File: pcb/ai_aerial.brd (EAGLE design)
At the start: 73 x 73 mm, 34 parts

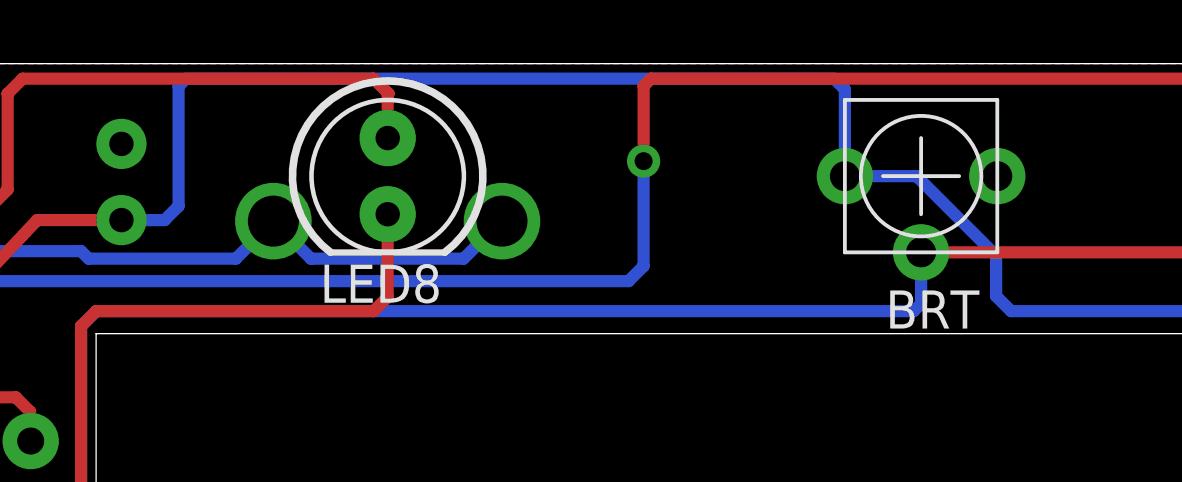
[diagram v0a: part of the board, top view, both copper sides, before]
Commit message: fixing trace error
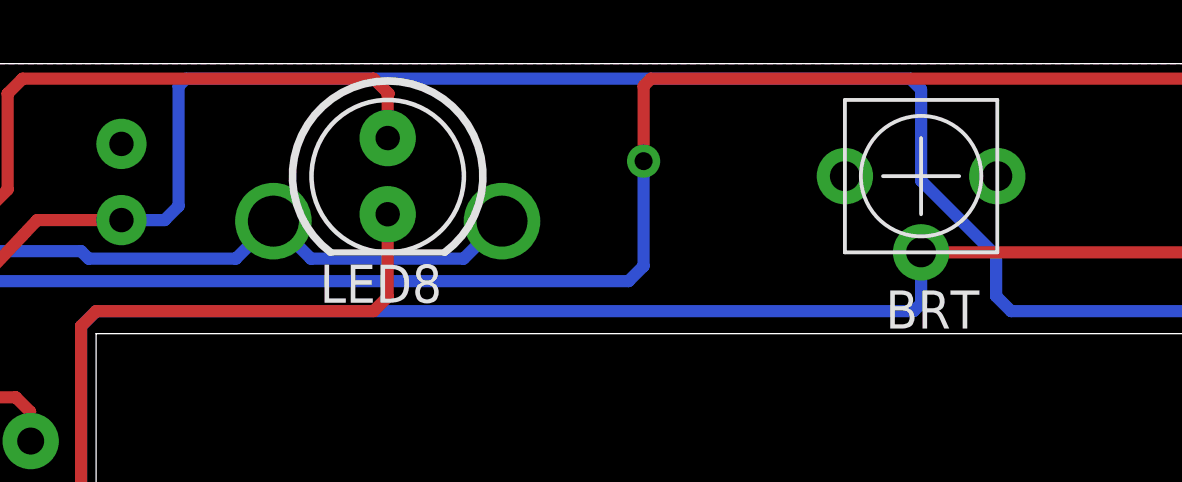
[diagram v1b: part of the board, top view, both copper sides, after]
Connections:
- net VBAT: no longer BRT.3
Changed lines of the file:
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@@
 <?xml version="1.0" encoding="utf-8"?>
 <!DOCTYPE eagle SYSTEM "eagle.dtd">
-<eagle version="7.1.0">
+<eagle version="6.5.0">
 <drawing>
 <settings>
@@
 <pass name="Default">
 <param name="RoutingGrid" value="50mil"/>
-<param name="AutoGrid" value="1"/>
-<param name="Efforts" value="0"/>
-<param name="TopRouterVariant" value="1"/>
 <param name="tpViaShape" value="round"/>
 <param name="PrefDir.1" value="|"/>
@@
 <contactref element="R5" pad="P$2"/>
 <contactref element="Q4" pad="3"/>
-<contactref element="BRT" pad="3"/>
 <contactref element="BAT1" pad="PWR@1"/>
 <contactref element="BAT1" pad="PWR@2"/>
@@
 <wire x1="3.6" y1="66.05" x2="5.4" y2="66.05" width="0.4064" layer="1"/>
 <wire x1="5.4" y1="66.05" x2="7.035" y2="67.785" width="0.4064" layer="1"/>
-<wire x1="33.6" y1="72.5" x2="12" y2="72.5" width="0.4064" layer="16"/>
+<wire x1="36.14" y1="72.5" x2="12" y2="72.5" width="0.4064" layer="16"/>
 <wire x1="12" y1="72.5" x2="11.75" y2="72.25" width="0.4064" layer="16"/>
 <wire x1="11.75" y1="72.25" x2="11.75" y2="68.25" width="0.4064" layer="16"/>
@@
 <wire x1="64.5" y1="8.75" x2="64.5" y2="9.5" width="0.4064" layer="16"/>
 <wire x1="9.845" y1="67.785" x2="7.035" y2="67.785" width="0.4064" layer="1"/>
-<wire x1="33.96" y1="69.25" x2="33.96" y2="72.14" width="0.4064" layer="16"/>
-<wire x1="33.96" y1="72.14" x2="33.6" y2="72.5" width="0.4064" layer="16"/>
-<wire x1="33.96" y1="69.25" x2="36.35" y2="69.25" width="0.4064" layer="16"/>
-<wire x1="36.35" y1="69.25" x2="39" y2="66.6" width="0.4064" layer="16"/>
+<wire x1="36.5" y1="72.14" x2="36.14" y2="72.5" width="0.4064" layer="16"/>
+<wire x1="36.5" y1="69.1" x2="39" y2="66.6" width="0.4064" layer="16"/>
 <wire x1="39" y1="66.6" x2="39" y2="65.25" width="0.4064" layer="16"/>
 <via x="47.25" y="5.25" extent="1-16" drill="0.6"/>
+<wire x1="36.5" y1="72.14" x2="36.5" y2="69.1" width="0.4064" layer="16"/>
 </signal>
 <signal name="N$6">
